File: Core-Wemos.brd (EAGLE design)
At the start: 86.5 x 100 mm, 49 parts, among them CON1 0.100, J1 2.1mm, J2 2mm, J3 IO4, Q1 BSS138, Q2 BSS138, Q3 BSS138, Q4 BSS138, Q5 BSS138, Q6 BSS138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

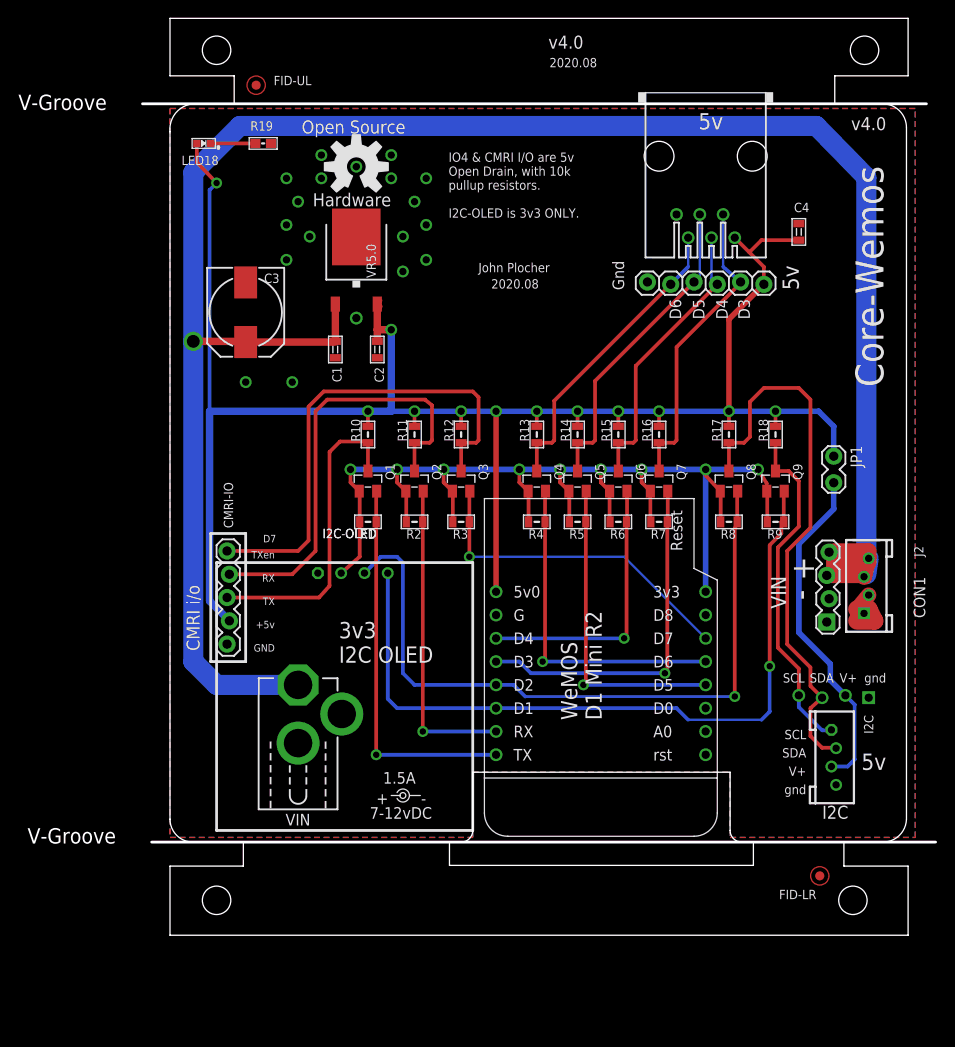
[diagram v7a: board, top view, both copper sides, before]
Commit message: normalized values
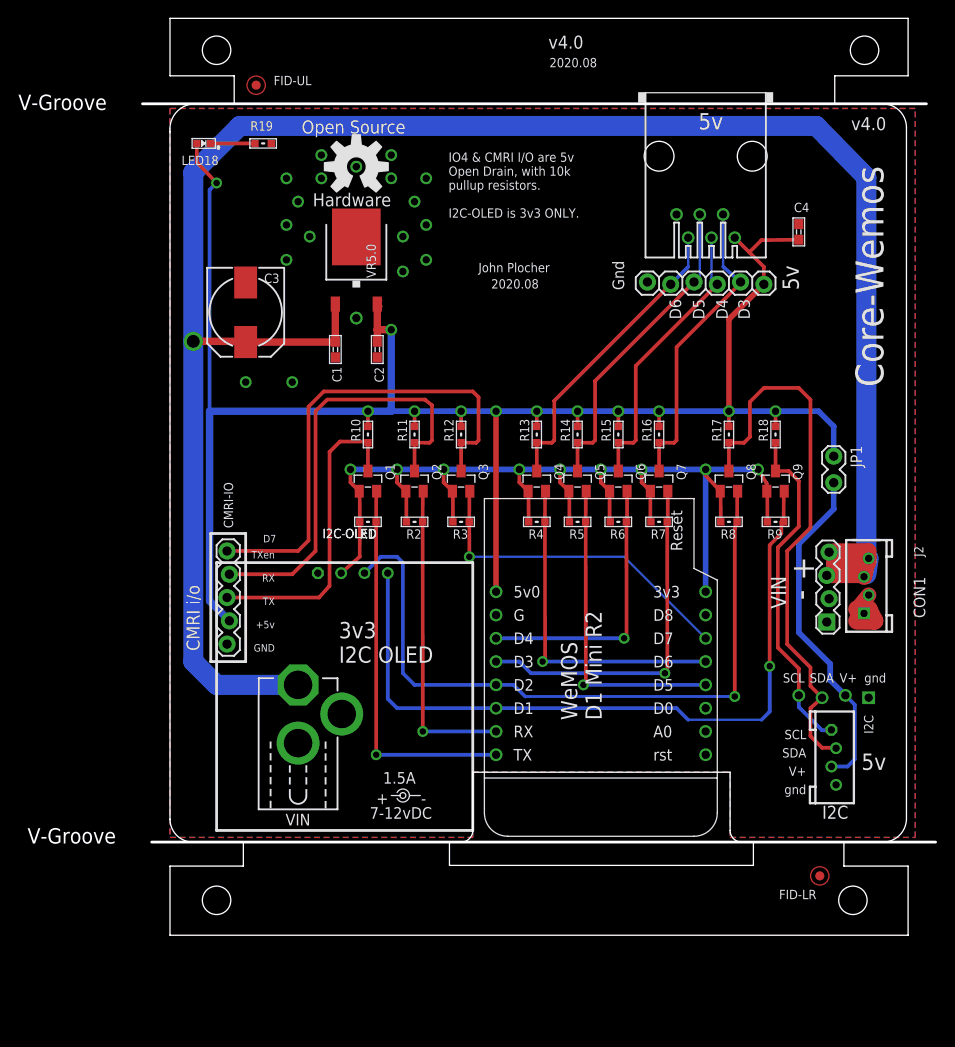
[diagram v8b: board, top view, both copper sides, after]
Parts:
- BOARD: value BOARD80X80 -> BOARD
- C1, C2, C4: device SPCoast:0805-CAP -> SPCoast:0603-CAP
- C3: value 150uF -> 220uF
- I2C: value CONNECTOR-I2CLEFT -> I2C
- I2C-OLED: value OLED -> I2C
- J3: value IO4 -> RJ12/6
- OSHW1: value OSHW-LOGOL -> OSHW
- R1, R10, R11, R12, R13, R14, R15, R16, R17, R18, R2, R3, R4, R5, R6, R7, R8, R9: device SPCoast:0805-RES -> SPCoast:0603-RES
